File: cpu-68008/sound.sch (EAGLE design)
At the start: 36 parts, among them IC101 GAL22V10D, IC102 74HCT175N, IC201 74HC73, IC202 YM3812, IC203 YM3014B, IC204 AY-3-8910, IC301 TL062, J301 RCALOCK

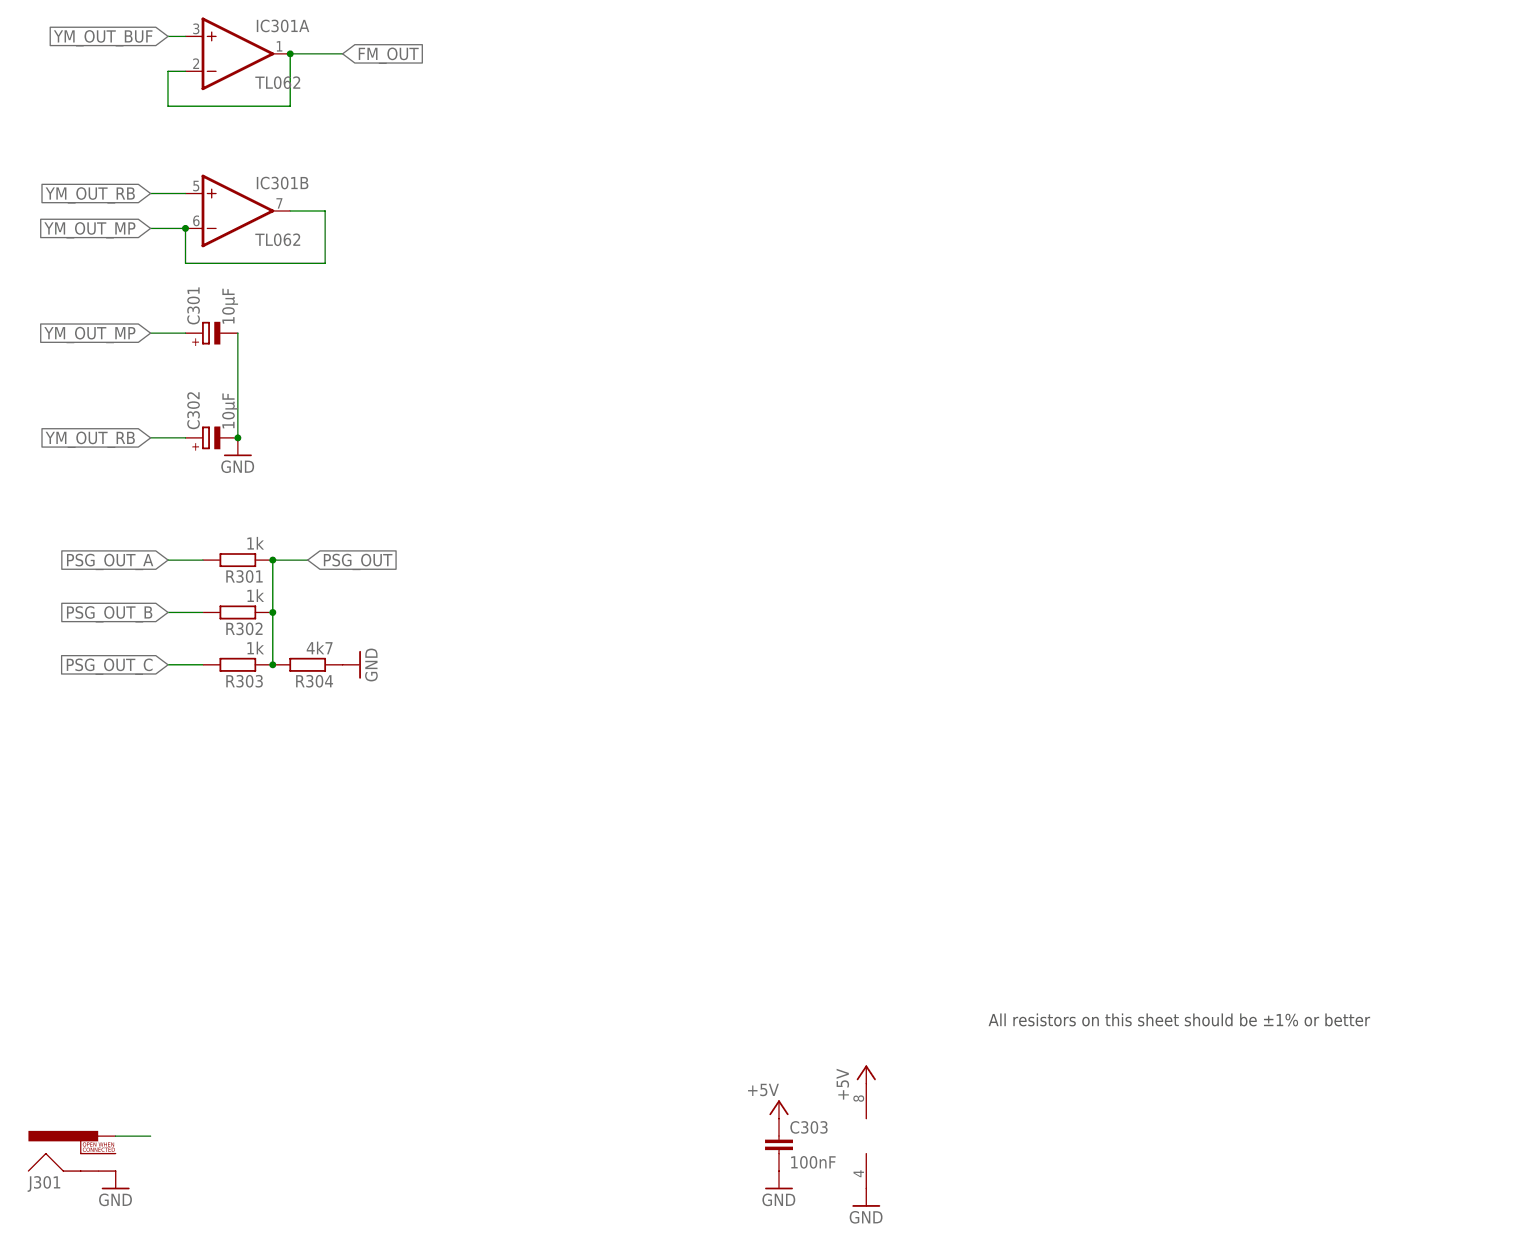
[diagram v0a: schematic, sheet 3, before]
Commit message: added analog component to mix on sound card
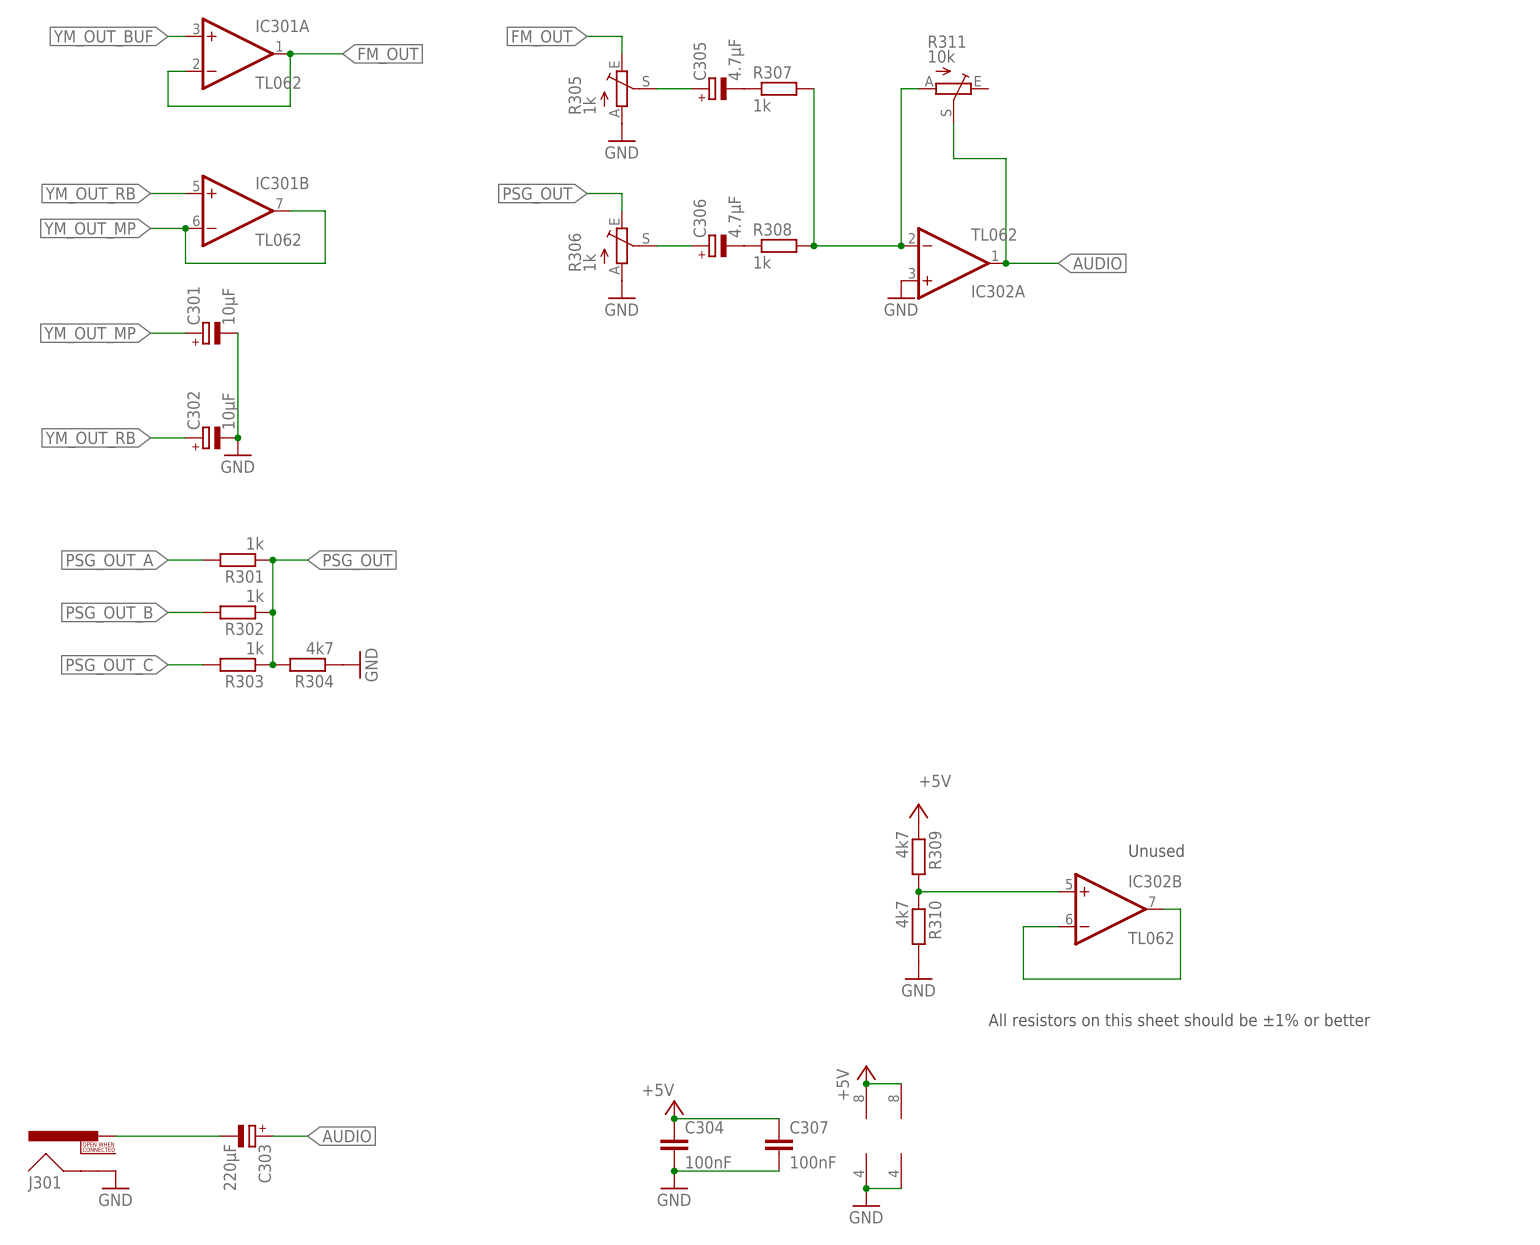
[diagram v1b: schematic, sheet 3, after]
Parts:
- added C304, C307: 100nF, rcl:C-EUC0805
- added C305, C306: 4.7µF, rcl:CPOL-EUE2-5
- added IC302: TL062, linear:TL062P
- added R305, R306: 1k, pot:TRIM_EU-PT10S
- added R307, R308: 1k, rcl:R-EU_R2012
- added R309, R310: 4k7, rcl:R-EU_R2012
- added R311: 10k, pot:TRIM_EU-PT10S
- C303: value 100nF -> 220µF; device rcl:C-EUC0805 -> rcl:CPOL-EUE2.5-6; MOUSER 710-885012207072 -> 710-860020273009
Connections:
- new net AUDIO: C303.+, IC302A.OUT, R311.S
- new net N$1: C305.+, R305.S
- new net N$10: C305.-, R307.1
- new net N$11: C306.-, R308.1
- new net N$12: IC302A.-IN, R307.2, R308.2, R311.A
- new net N$13: IC302B.-IN, IC302B.OUT
- new net N$15: IC302B.+IN, R309.2, R310.1
- net +5V: now also C304.1, C307.1, IC302P.V+, R309.1; no longer C303.1
- net FM_OUT: now also R305.E
- net GND: now also C304.2, C307.2, IC302A.+IN, IC302P.V-, R305.A, R306.A, R310.2; no longer C303.2
- net N$4: now also C303.-
- net N$7: now also C306.+, R306.S; no longer IC101.IN7
- net PSG_OUT: now also R306.E
- net SLOT_A0: now also IC101.IN7
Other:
- note added: "Unused"

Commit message: start working on adding midi in/out to sound board
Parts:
- removed LED101: (no value), led:LEDCHIPLED_1206
- removed R101: 3k, rcl:R-EU_R2012
- added CN401, CN402: DIN5, SparkFun-Connectors:DIN5
- IC301, IC302, VR301, VR302, VR303: SPICEPREFIX (none) -> J
- renumbered J301 to CN301, R305 to VR301, R306 to VR303, R311 to VR302
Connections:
- removed net N$3: LED101.A, R101.2
- removed net N$8: IC101.IN8
- net !YM_IRQ: no longer LED101.C
- net +5V: no longer R101.1
- net SLOT_A9: now also IC101.IN8
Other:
- note added: "CN401: MIDI In CN402: MIDI Out"

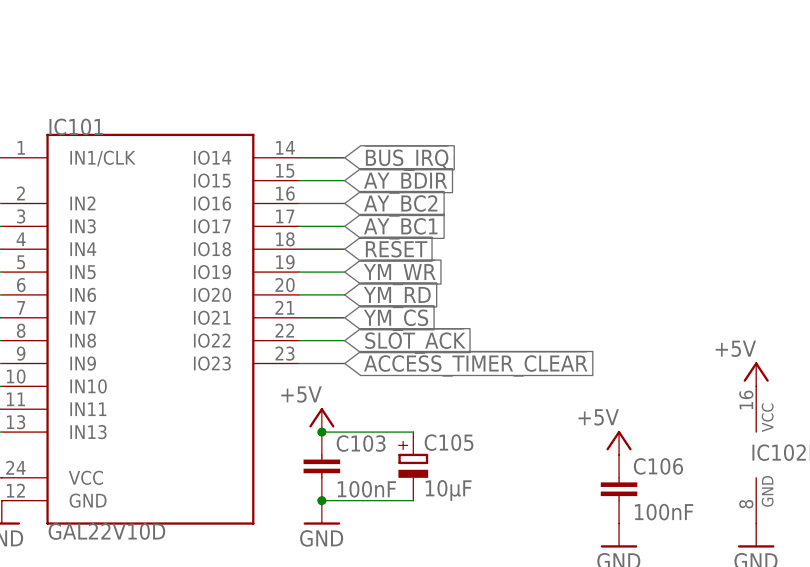
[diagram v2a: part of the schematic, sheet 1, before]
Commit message: cleaned up routing for sound board a bit, moved some things in preparation of adding midi interface
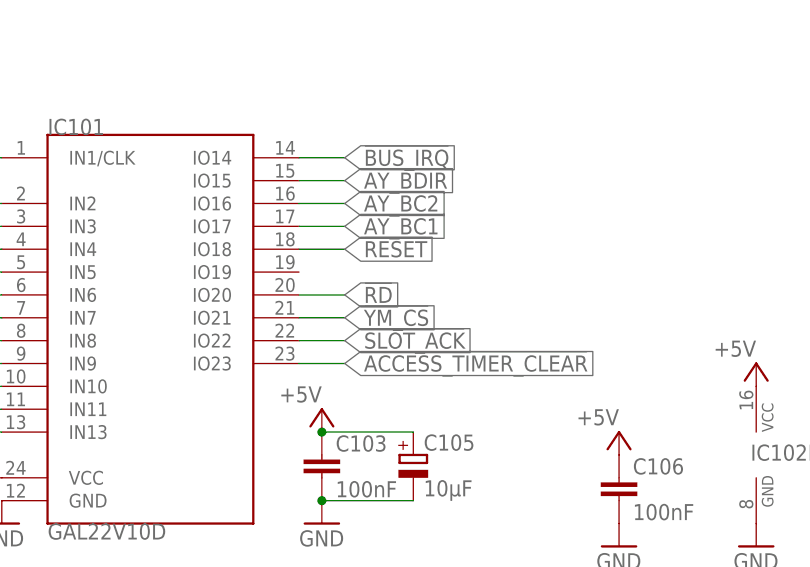
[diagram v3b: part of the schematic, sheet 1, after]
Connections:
- net !YM_RD renamed !RD
- removed net !YM_WR: IC101.IO19, IC202.!WR
- net SLOT_R/!W!: now also IC202.!WR
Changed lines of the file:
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@@
 </segment>
 </net>
-<net name="!YM_RD" class="0">
+<net name="!RD" class="0">
 <segment>
 <pinref part="IC101" gate="G$1" pin="IO20"/>
@@
 <wire x1="91.44" y1="40.64" x2="86.36" y2="40.64" width="0.1524" layer="91"/>
 <label x="91.44" y="40.64" size="1.778" layer="95" xref="yes"/>
-</segment>
-</net>
-<net name="!YM_WR" class="0">
-<segment>
-<pinref part="IC101" gate="G$1" pin="IO19"/>
-<wire x1="91.44" y1="35.56" x2="86.36" y2="35.56" width="0.1524" layer="91"/>
-<label x="91.44" y="35.56" size="1.778" layer="95" xref="yes"/>
 </segment>
 </net>
@@
 </segment>
 </bus>
-<bus name="SLOT_A[0],SLOT_D[0..7],!YM_CS,!YM_RD">
+<bus name="!RD,SLOT_A[0],SLOT_D[0..7],SLOT_R/!W!,!YM_CS">
 <segment>
 <wire x1="30.48" y1="167.64" x2="30.48" y2="127" width="0.762" layer="92"/>
@@
 </segment>
 </net>
-<net name="!YM_WR" class="0">
+<net name="SLOT_R/!W!" class="0">
 <segment>
 <pinref part="IC202" gate="G$1" pin="!WR"/>
@@
 </segment>
 </net>
-<net name="!YM_RD" class="0">
+<net name="!RD" class="0">
 <segment>
 <pinref part="IC202" gate="G$1" pin="!RD"/>

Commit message: finished midi circuit frontends
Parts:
- removed CN401, CN402: DIN5, SparkFun-Connectors:DIN5
- removed IC204: AY-3-8910, 68komputer:AY-3-8910
- added C401, C402, C403: 100nF, rcl:C-EUC0805
- added C404: 10µF, rcl:CPOL-EUSMCB
- added D401: 1N914, diode:1N4148DO35-10
- added IC401: 74HCT14N, 74xx-eu:74HCT14N
- added IC402: TL16C550D, 68komputer:TL16C550DLQFP-48
- added J401, J402: DIN5, SparkFun-Connectors:DIN5
- added OK401: H11L1M, optocoupler:H11L1M
- added QG202: (no value), crystal:XO-8
- added R401, R403: 220R, rcl:R-EU_R2012
- added R402: 4k7, rcl:R-EU_R2012
- IC201: value 74HC73 -> YM3812; device 74xx-eu:74LS73N -> 68komputer:YM3812DIL24
- IC202: value YM3812 -> YM3014B; device 68komputer:YM3812DIL24 -> 68komputer:YM3014BDIL8
- IC203: value YM3014B -> AY-3-8910; device 68komputer:YM3014BDIL8 -> 68komputer:AY-3-8910
- renumbered CN301 to J301, VR301 to R305, VR302 to R311, VR303 to R306
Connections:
- removed net !CLK_B: IC201A.!Q, IC201A.J
- removed net !CLK_C: IC201B.!Q, IC201B.J
- removed net CLK_C: IC201B.K, IC201B.Q
- removed net N$9: IC101.IN9
- new net !MIDI_UART_CS: IC101.IO19, IC402.!CS2
- new net MIDI_IRQ: IC101.IN9, IC402.INTRPT
- new net MIDI_RESET: IC401C.O, IC402.MR
- new net MIDI_RX: IC402.SIN, OK401.OUT, R402.1
- new net MIDI_RX_+: D401.A, J401.5, OK401.C
- new net MIDI_RX_-: D401.C, OK401.A, R401.2
- new net MIDI_TX: IC401A.I, IC402.SOUT
- new net MIDI_TX_-: IC401B.O, J402.5
- new net N$14: J401.4, R401.1
- new net N$16: IC401A.O, IC401B.I
- new net N$17: J402.4, R403.1
- new net N$3: IC402.!BAUDOUT, IC402.RCLK
- new net N$8: IC402.CS0, IC402.CS1
- net !RD: now also IC201.!RD, IC402.!RD1; no longer IC202.!RD
- net !RESET: now also IC201.!RESET, IC203.!RESET, IC401C.I; no longer IC202.!RESET, IC204.!RESET
- net !SLOT_AS: now also IC402.!ADS
- net !YM_CS: now also IC201.!CS; no longer IC202.!CS
- net !YM_IRQ: now also IC201.!IRQ; no longer IC202.!IRQ
- net +5V: now also C401.1, C402.1, C403.1, C404.+, IC201.VCC, IC202.VDD, IC203.A8, IC203.VCC, IC401P.VCC, OK401.VCC, QG202.VCC, R402.2, R403.2; no longer IC201A.CL, IC201B.CL, IC201P.VCC, IC202.VCC, IC203.VDD, IC204.A8, IC204.VCC
- net AY_BC1: now also IC203.BC1; no longer IC204.BC1
- net AY_BC2: now also IC203.BC2; no longer IC204.BC2
- net AY_BDIR: now also IC203.BDIR; no longer IC204.BDIR
- net CLK_A: now also IC201.CLK; no longer IC201A.CLK, IC202.CLK
- net CLK_B: now also IC203.CLK, IC402.XIN, QG202.OUT; no longer IC201A.K, IC201A.Q, IC201B.CLK, IC204.CLK
- net GND: now also C401.2, C402.2, C403.2, C404.-, IC201.GND, IC203.!A9, IC401D.I, IC401E.I, IC401F.I, IC401P.GND, J402.2, OK401.GND, QG202.GND; no longer IC201P.GND, IC204.!A9, IC204.GND
- net IOA0: now also IC203.IOA0; no longer IC204.IOA0
- net IOA1: now also IC203.IOA1; no longer IC204.IOA1
- net IOA2: now also IC203.IOA2; no longer IC204.IOA2
- net IOA3: now also IC203.IOA3; no longer IC204.IOA3
- net IOA4: now also IC203.IOA4; no longer IC204.IOA4
- net IOA5: now also IC203.IOA5; no longer IC204.IOA5
- net IOA6: now also IC203.IOA6; no longer IC204.IOA6
- net IOA7: now also IC203.IOA7; no longer IC204.IOA7
- net IOB0: now also IC203.IOB0; no longer IC204.IOB0
- net IOB1: now also IC203.IOB1; no longer IC204.IOB1
- net IOB2: now also IC203.IOB2; no longer IC204.IOB2
- net IOB3: now also IC203.IOB3; no longer IC204.IOB3
- net IOB4: now also IC203.IOB4; no longer IC204.IOB4
- net IOB5: now also IC203.IOB5; no longer IC204.IOB5
- net IOB6: now also IC203.IOB6; no longer IC204.IOB6
- net IOB7: now also IC203.IOB7; no longer IC204.IOB7
- net PSG_OUT_A: now also IC203.OUTA; no longer IC204.OUTA
- net PSG_OUT_B: now also IC203.OUTB; no longer IC204.OUTB
- net PSG_OUT_C: now also IC203.OUTC; no longer IC204.OUTC
- net SLOT_A0: now also IC201.A0, IC402.A0; no longer IC202.A0
- net SLOT_A1: now also IC402.A1
- net SLOT_A2: now also IC402.A2
- net SLOT_D0: now also IC201.D0, IC203.DA0, IC402.D0; no longer IC202.D0, IC204.DA0
- net SLOT_D1: now also IC201.D1, IC203.DA1, IC402.D1; no longer IC202.D1, IC204.DA1
- net SLOT_D2: now also IC201.D2, IC203.DA2, IC402.D2; no longer IC202.D2, IC204.DA2
- net SLOT_D3: now also IC201.D3, IC203.DA3, IC402.D3; no longer IC202.D3, IC204.DA3
- net SLOT_D4: now also IC201.D4, IC203.DA4, IC402.D4; no longer IC202.D4, IC204.DA4
- net SLOT_D5: now also IC201.D5, IC203.DA5, IC402.D5; no longer IC202.D5, IC204.DA5
- net SLOT_D6: now also IC201.D6, IC203.DA6, IC402.D6; no longer IC202.D6, IC204.DA6
- net SLOT_D7: now also IC201.D7, IC203.DA7, IC402.D7; no longer IC202.D7, IC204.DA7
- net SLOT_R/!W!: now also IC201.!WR, IC402.!WR1; no longer IC202.!WR
- net YM_DAC_CLK: now also IC201.DACCLK, IC202.CLK; no longer IC202.DACCLK, IC203.CLK
- net YM_DAC_DATA: now also IC201.DACMO, IC202.DATA; no longer IC202.DACMO, IC203.DATA
- net YM_DAC_SY: now also IC201.DACSY, IC202.SYNC; no longer IC202.DACSY, IC203.SYNC
- net YM_OUT_BUF: now also IC202.BUFF; no longer IC203.BUFF
- net YM_OUT_MP: now also IC202.MP; no longer IC203.MP
- net YM_OUT_RB: now also IC202.RB; no longer IC203.RB
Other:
- note added: "CLK_A: 3.579545 MHz (YM) CLK_B: 2.0 MHz (AY, MIDI)"
- note removed: "CLK_A: 3.579545 MHz CLK_B: 1.7897725 MHz CLK_C: 0.89488625 MHz"
